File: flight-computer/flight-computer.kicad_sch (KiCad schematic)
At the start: 7 parts, among them J1 Screw_Terminal_01x02, SW1 SW_SPST, U1 MPU6050, U2 BMP180, U3 ESP32_DEVKIT

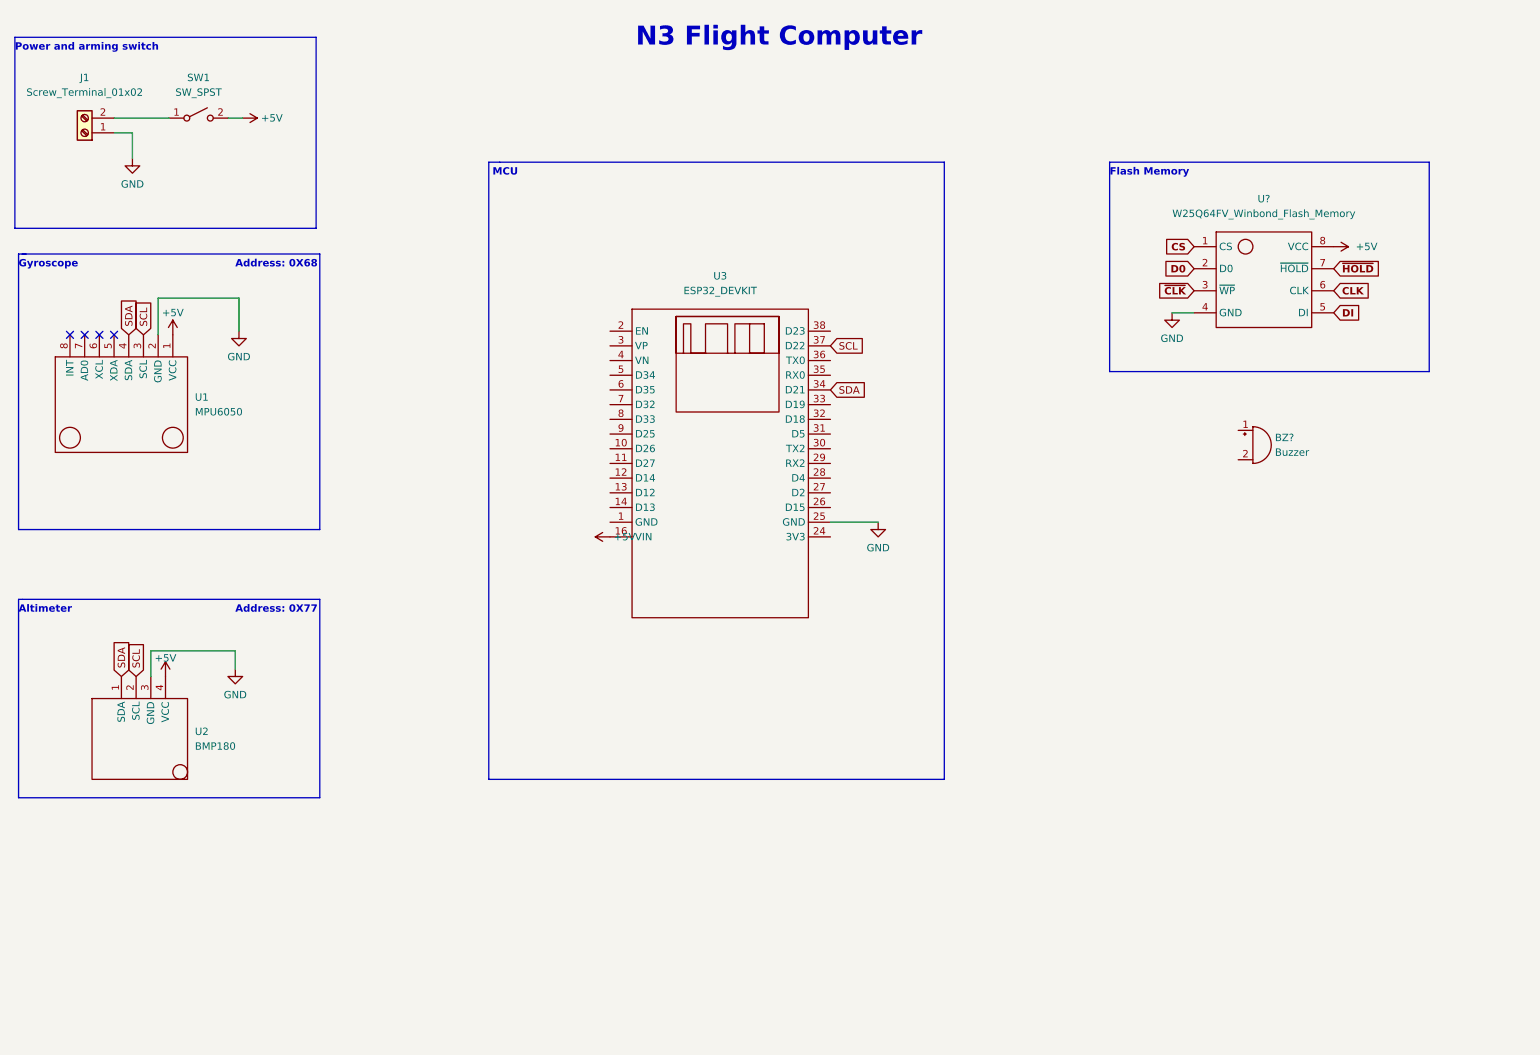
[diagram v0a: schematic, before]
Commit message: added PCB footprints for altimeter and gyroscope
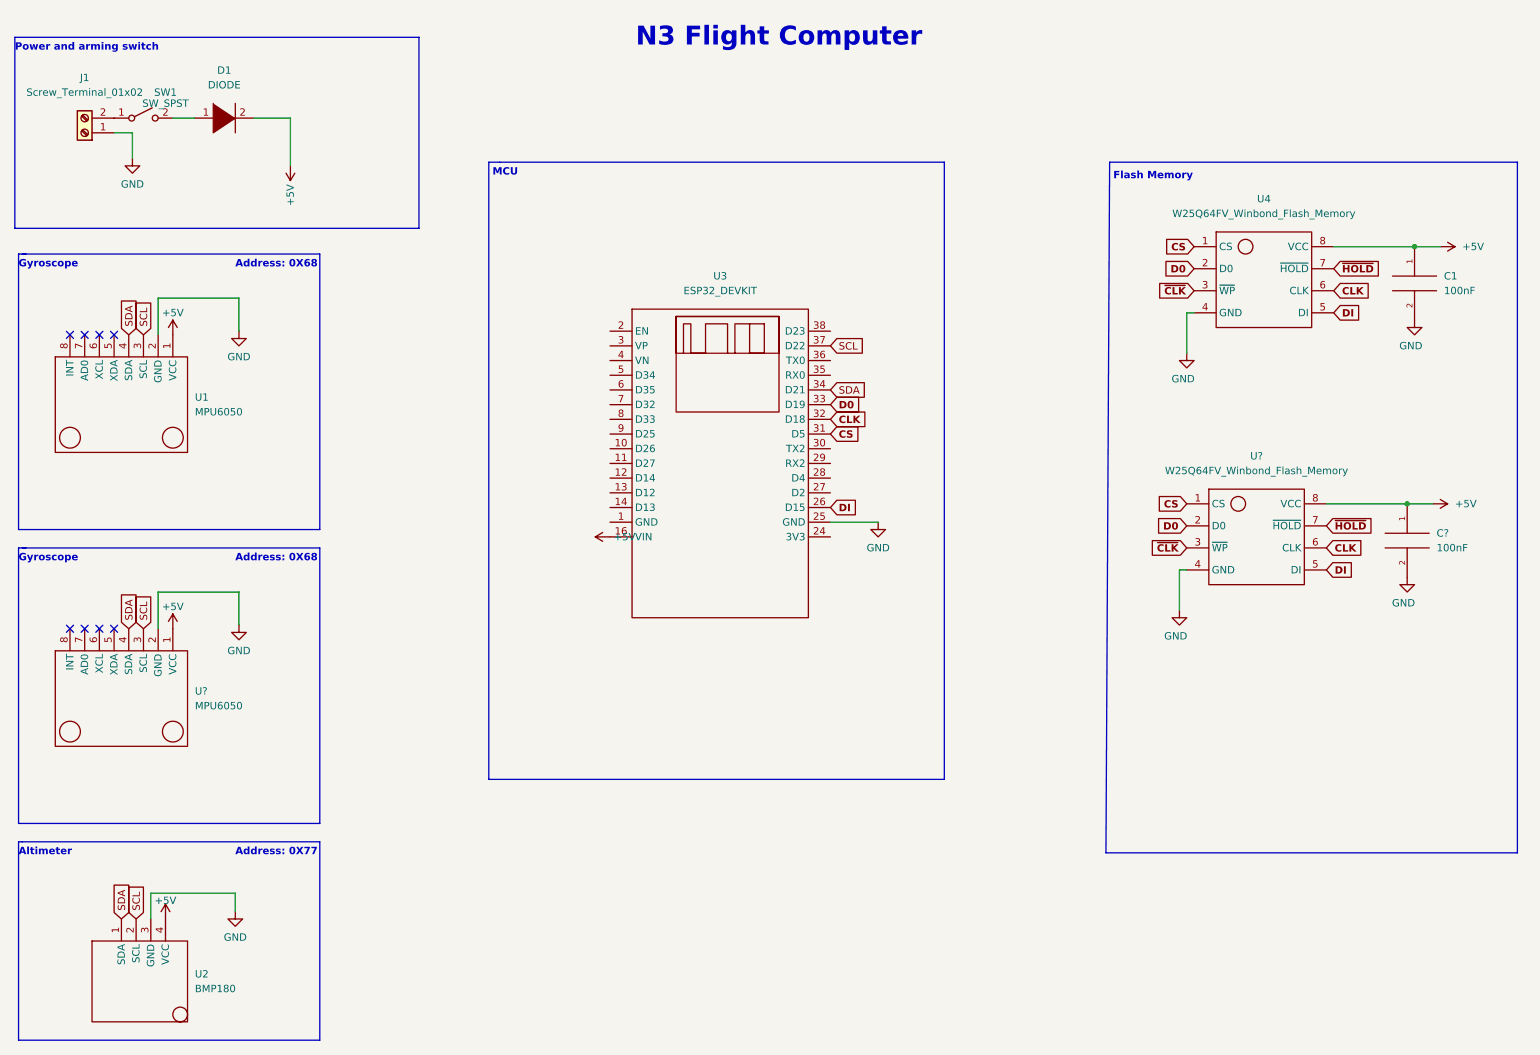
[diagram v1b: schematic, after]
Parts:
- removed BZ?: Buzzer, symbol Device:Buzzer
- added C1, C?: 100nF, Capacitor_SMD:C_0805_2012Metric, symbol pspice:CAP
- added D1: DIODE, Diode_THT:D_A-405_P12.70mm_Horizontal, symbol pspice:DIODE
- added U?: W25Q64FV_Winbond_Flash_Memory, Package_SO:HTSOP-8-1EP_3.9x4.9mm_P1.27mm_EP2.4x3.2mm, symbol modules:W25Q64FV_Winbond_Flash_Memory
- added U?: MPU6050, custom-footprints:MPU6050, symbol modules:MPU6050
- J1: footprint (none) -> TerminalBlock:TerminalBlock_bornier-2_P5.08mm
- SW1: footprint (none) -> custom-footprints:Rocker_Switch_SPST
- U1: footprint (none) -> custom-footprints:MPU6050
- U2: footprint (none) -> custom-footprints:BMP180
- U3: footprint (none) -> custom-footprints:ESP32_DEVKIT
- U4: renamed from U?; footprint (none) -> Package_SO:HTSOP-8-1EP_3.9x4.9mm_P1.27mm_EP2.4x3.2mm
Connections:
- net +5V: now also C1.1, C?.1, D1.2 (A), U?.1 (VCC), U?.8 (VCC); no longer SW1.2 (B)
- net CLK: now also U3.32 (D18), U?.6 (CLK)
- net CS: now also U3.31 (D5), U?.1 (CS)
- net D0: now also U3.33 (D19), U?.2 (D0)
- net DI: now also U3.26 (D15), U?.5 (DI)
- net GND: now also C1.2, C?.2, U?.2 (GND), U?.4 (GND)
- net SCL: now also U?.3 (SCL)
- net SDA: now also U?.4 (SDA)
- net ~{CLK}: now also U?.3 (~{WP})
- net ~{HOLD}: now also U?.7 (~{HOLD})
- new net: D1.1 (K), SW1.2 (B)
- no-connect marks 4 -> 8
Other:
- moved on the sheet: SW1, U2

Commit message: added mounting holes for sensors
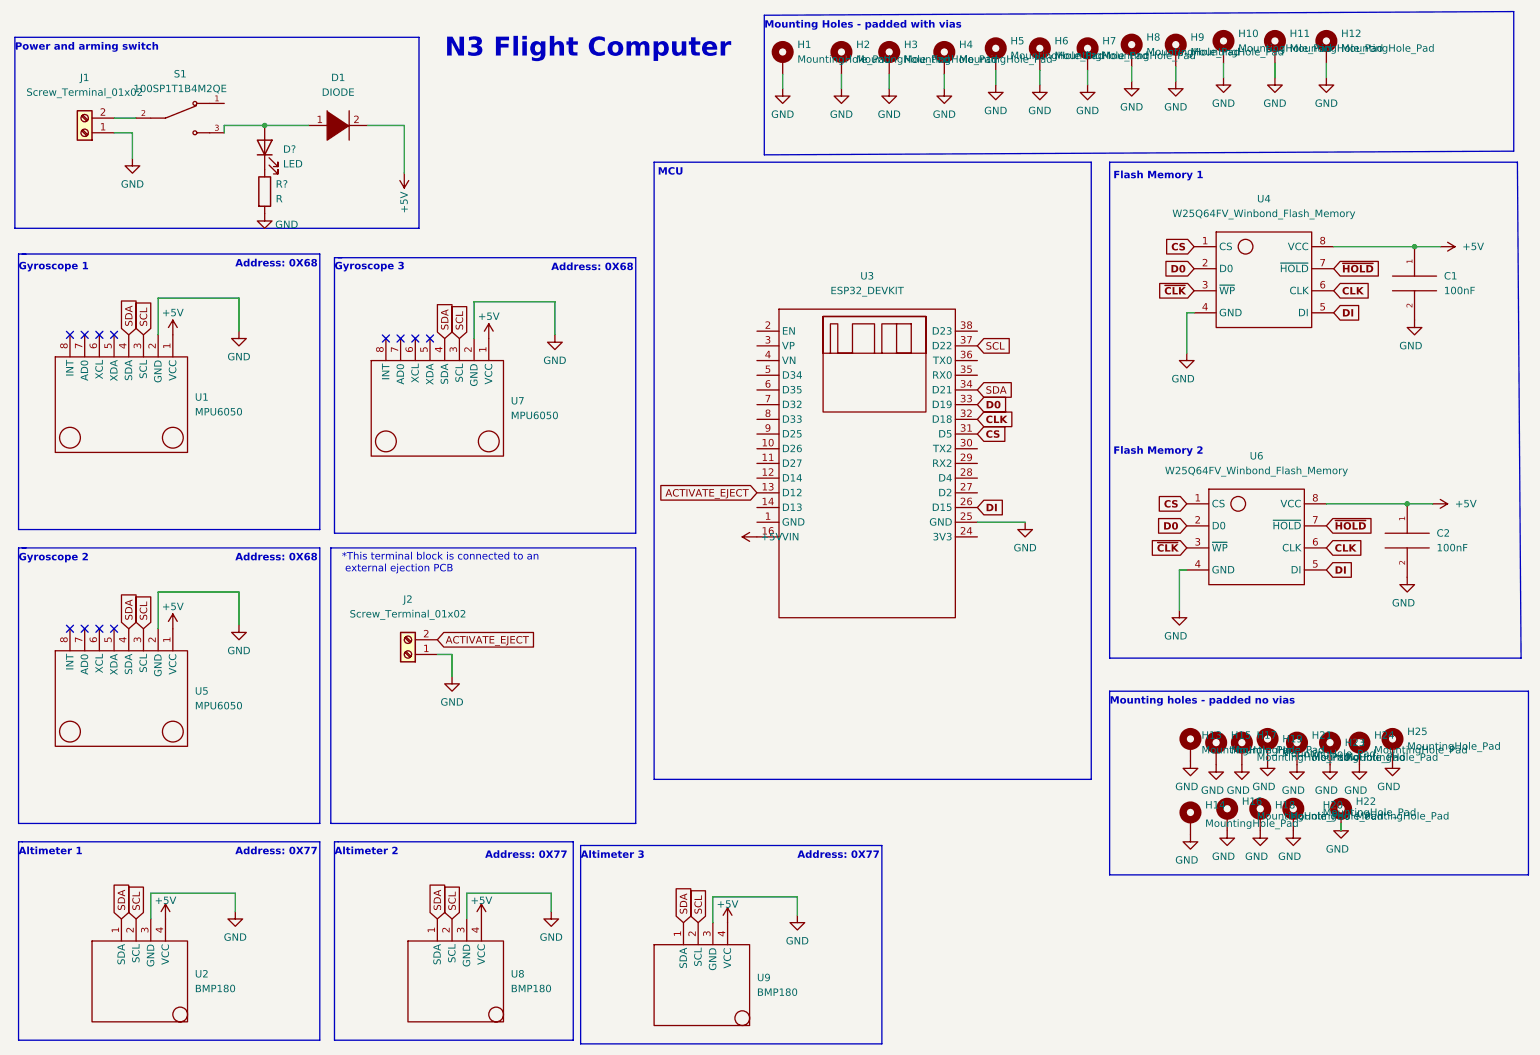
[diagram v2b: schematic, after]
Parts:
- removed SW1: SW_SPST, custom-footprints:Rocker_Switch_SPST, symbol Switch:SW_SPST
- added D?: LED, LED_SMD:LED_0805_2012Metric, symbol Device:LED
- added H1, H10, H11, H12, H2, H3, H4, H5, H6, H7, H8, H9: MountingHole_Pad, MountingHole:MountingHole_3.2mm_M3_Pad_Via, symbol Mechanical:MountingHole_Pad
- added H13, H14, H15, H16, H17, H18, H19, H20, H21, H22, H23, H24, H25: MountingHole_Pad, MountingHole:MountingHole_3.2mm_M3_Pad_TopOnly, symbol Mechanical:MountingHole_Pad
- added J2: Screw_Terminal_01x02, TerminalBlock:TerminalBlock_bornier-2_P5.08mm, symbol Connector:Screw_Terminal_01x02
- added R?: R, Resistor_SMD:R_0805_2012Metric, symbol Device:R
- added S1: 100SP1T1B4M2QE, spdt_toggle_switch:SW_100SP1T1B4M2QE, symbol toggle-switch:100SP1T1B4M2QE
- added U7: MPU6050, custom-footprints:MPU6050, symbol modules:MPU6050
- added U8, U9: BMP180, custom-footprints:BMP180, symbol modules:BMP180
- gave numbers to parts that had none: 3
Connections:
- net +5V: now also U7.1 (VCC), U8.4 (VCC), U9.4 (VCC)
- net GND: now also H1.1, H10.1, H11.1, H12.1, H13.1, H14.1, H15.1, H16.1, H17.1, H18.1, H19.1, H2.1, H20.1, H21.1, H22.1, H23.1, H24.1, H25.1, H3.1, H4.1, H5.1, H6.1, H7.1, H8.1, H9.1, J2.1 (Pin_1), R?.2, U7.2 (GND), U8.3 (GND), U9.3 (GND)
- net SCL: now also U7.3 (SCL), U8.2 (SCL), U9.2 (SCL)
- net SDA: now also U7.4 (SDA), U8.1 (SDA), U9.1 (SDA)
- net at J1.2 (Pin_2): now also S1.2
- net at D1.1 (K): now also D?.2 (A), S1.3
- net ACTIVATE_EJECT: now reaches U3.13 (D12)
- net ACTIVATE_EJECT: now also J2.2 (Pin_2)
- new net: D?.1 (K), R?.1
- no-connect marks 8 -> 12
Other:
- note added: "*This terminal block is connected to an external ejection PCB"
- note added: "Altimeter 1"
- note added: "Altimeter 2"
- note added: "Altimeter 3"
- note added: "Flash Memory 1"
- note added: "Flash Memory 2"
- note added: "Gyroscope 1"
- note added: "Gyroscope 2"
- note added: "Gyroscope 3"
- note added: "Mounting Holes - padded with vias"
- note added: "Mounting holes - padded no vias"
- note removed: "Altimeter"
- note removed: "Flash Memory"
- note removed: "Gyroscope"
- moved on the sheet: D1, U3
